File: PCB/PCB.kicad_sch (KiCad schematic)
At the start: 51 parts, among them J1 Conn_01x02_Socket, J2 Conn_01x02_Pin, J3 Conn_01x02_Pin, J4 Conn_01x02_Socket, J5 Programming Pin, J6 Programming Pin, J7 Programming Pin, J8 Programming Pin, U1 STM32L476RGTx, U2 FGPMMOPA6H, U4 TPS63001DRCR, U5 LM2735XMF/NOPB, U8 LM386, U9 MAX7375AXR805

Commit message: Add files via upload
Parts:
- removed FB1, FB4: FerriteBead, Ferrite_THT:LairdTech_28C0236-0JW-10, symbol Device:FerriteBead
- added R4, R5: 0 Ohms, symbol Device:R_US
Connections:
- net Earth: now also R4.1, R5.1
- net VDDA Connection: now also R4.2
- net VDDA GND Connection: now also R5.2
- net at U1.14 (PA0): no longer U2.P$10 (RX)
- net at U1.15 (PA1): no longer U2.P$9 (TX)
- net at U1.42 (PA9): now also U2.P$10 (RX)
- net at U1.43 (PA10): now also U2.P$9 (TX)
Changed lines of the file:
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@@
 	)
 	(no_connect
+		(at 186.69 80.01)
+	)
+	(no_connect
 		(at 186.69 153.67)
 	)
@@
 	)
 	(no_connect
-		(at 186.69 102.87)
-	)
-	(no_connect
 		(at 151.13 110.49)
 	)
@@
 	)
 	(no_connect
-		(at 186.69 105.41)
-	)
-	(no_connect
 		(at 151.13 138.43)
 	)
@@
 	)
 	(no_connect
+		(at 186.69 82.55)
+	)
+	(no_connect
 		(at 104.14 142.24)
 	)
@@
 	(wire
 		(pts
+			(xy 186.69 102.87) (xy 194.31 102.87)
+		)
+		(stroke
+			(width 0)
+			(type default)
+		)
+	)
+	(wire
+		(pts
 			(xy 194.31 179.07) (xy 67.31 179.07)
 		)
@@
 	(wire
 		(pts
+			(xy 190.5 105.41) (xy 190.5 177.8)
+		)
+		(stroke
+			(width 0)
+			(type default)
+		)
+	)
+	(wire
+		(pts
 			(xy 220.98 55.88) (xy 243.84 55.88)
 		)
@@
 	(wire
 		(pts
+			(xy 186.69 105.41) (xy 190.5 105.41)
+		)
+		(stroke
+			(width 0)
+			(type default)
+		)
+	)
+	(wire
+		(pts
 			(xy 181.61 24.13) (xy 223.52 24.13)
 		)
@@
 	(wire
 		(pts
-			(xy 190.5 82.55) (xy 190.5 177.8)
-		)
-		(stroke
-			(width 0)
-			(type default)
-		)
-	)
-	(wire
-		(pts
 			(xy 66.04 87.63) (xy 83.82 87.63)
 		)
@@
 	(wire
 		(pts
-			(xy 194.31 80.01) (xy 194.31 179.07)
-		)
-		(stroke
-			(width 0)
-			(type default)
-		)
-	)
-	(wire
-		(pts
 			(xy 43.18 46.99) (xy 48.26 46.99)
 		)
@@
 	(wire
 		(pts
+			(xy 194.31 102.87) (xy 194.31 179.07)
+		)
+		(stroke
+			(width 0)
+			(type default)
+		)
+	)
+	(wire
+		(pts
 			(xy 17.78 181.61) (xy 24.13 181.61)
 		)
@@
 	(wire
 		(pts
-			(xy 186.69 82.55) (xy 190.5 82.55)
-		)
-		(stroke
-			(width 0)
-			(type default)
-		)
-	)
-	(wire
-		(pts
 			(xy 171.45 72.39) (xy 176.53 72.39)
 		)
@@
 	(wire
 		(pts
-			(xy 186.69 80.01) (xy 194.31 80.01)
-		)
-		(stroke
-			(width 0)
-			(type default)
-		)
-	)
-	(wire
-		(pts
 			(xy 73.66 142.24) (xy 71.12 142.24)
 		)
@@
 	)
 	(symbol
-		(lib_id "Device:FerriteBead")
-		(at 245.11 153.67 90)
-		(unit 1)
-		(exclude_from_sim no)
-		(in_bom yes)
-		(on_board yes)
-		(dnp no)
-		(fields_autoplaced yes)
-		(property "Reference" "FB4"
-			(at 245.0592 146.05 90)
-			(effects
-				(font
-					(size 1.27 1.27)
-				)
-			)
-		)
-		(property "Value" "FerriteBead"
-			(at 245.0592 148.59 90)
-			(effects
-				(font
-					(size 1.27 1.27)
-				)
-			)
-		)
-		(property "Footprint" "Ferrite_THT:LairdTech_28C0236-0JW-10"
-			(at 245.11 155.448 90)
-			(effects
-				(font
-					(size 1.27 1.27)
-				)
-				(hide yes)
-			)
-		)
-		(property "Datasheet" "~"
-			(at 245.11 153.67 0)
-			(effects
-				(font
-					(size 1.27 1.27)
-				)
-				(hide yes)
-			)
-		)
-		(property "Description" ""
-			(at 245.11 153.67 0)
-			(effects
-				(font
-					(size 1.27 1.27)
-				)
-				(hide yes)
-			)
-		)
-		(pin "1"
-		)
-		(pin "2"
-		)
-		(instances
-			(project "PCB"
-				(path "/eb9a8801-b205-4599-90e8-b0089b4de1f9"
-					(reference "FB4")
-					(unit 1)
-				)
-			)
-		)
-	)
-	(symbol
 		(lib_id "Connector:Conn_01x02_Pin")
 		(at 21.59 10.16 270)
@@
 	)
 	(symbol
+		(lib_id "Device:R_US")
+		(at 245.11 153.67 90)
+		(unit 1)
+		(exclude_from_sim no)
+		(in_bom yes)
+		(on_board yes)
+		(dnp no)
+		(fields_autoplaced yes)
+		(property "Reference" "R5"
+			(at 245.11 147.32 90)
+			(effects
+				(font
+					(size 1.27 1.27)
+				)
+			)
+		)
+		(property "Value" "0 Ohms"
+			(at 245.11 149.86 90)
+			(effects
+				(font
+					(size 1.27 1.27)
+				)
+			)
+		)
+		(property "Footprint" ""
+			(at 245.364 152.654 90)
+			(effects
+				(font
+					(size 1.27 1.27)
+				)
+				(hide yes)
+			)
+		)
+		(property "Datasheet" "~"
+			(at 245.11 153.67 0)
+			(effects
+				(font
+					(size 1.27 1.27)
+				)
+				(hide yes)
+			)
+		)
+		(property "Description" "Resistor, US symbol"
+			(at 245.11 153.67 0)
+			(effects
+				(font
+					(size 1.27 1.27)
+				)
+				(hide yes)
+			)
+		)
+		(pin "2"
+		)
+		(pin "1"
+		)
+		(instances
+			(project "PCB"
+				(path "/eb9a8801-b205-4599-90e8-b0089b4de1f9"
+					(reference "R5")
+					(unit 1)
+				)
+			)
+		)
+	)
+	(symbol
 		(lib_id "Device:D_Schottky")
 		(at 252.73 17.78 180)
@@
 	)
 	(symbol
+		(lib_id "Device:R_US")
+		(at 243.84 143.51 90)
+		(unit 1)
+		(exclude_from_sim no)
+		(in_bom yes)
+		(on_board yes)
+		(dnp no)
+		(fields_autoplaced yes)
+		(property "Reference" "R4"
+			(at 243.84 137.16 90)
+			(effects
+				(font
+					(size 1.27 1.27)
+				)
+			)
+		)
+		(property "Value" "0 Ohms"
+			(at 243.84 139.7 90)
+			(effects
+				(font
+					(size 1.27 1.27)
+				)
+			)
+		)
+		(property "Footprint" ""
+			(at 244.094 142.494 90)
+			(effects
+				(font
+					(size 1.27 1.27)
+				)
+				(hide yes)
+			)
+		)
+		(property "Datasheet" "~"
+			(at 243.84 143.51 0)
+			(effects
+				(font
+					(size 1.27 1.27)
+				)
+				(hide yes)
+			)
+		)
+		(property "Description" "Resistor, US symbol"
+			(at 243.84 143.51 0)
+			(effects
+				(font
+					(size 1.27 1.27)
+				)
+				(hide yes)
+			)
+		)
+		(pin "2"
+		)
+		(pin "1"
+		)
+		(instances
+			(project ""
+				(path "/eb9a8801-b205-4599-90e8-b0089b4de1f9"
+					(reference "R4")
+					(unit 1)
+				)
+			)
+		)
+	)
+	(symbol
 		(lib_id "Buck-Boost Chip:TPS63001DRCR")
 		(at 66.04 62.23 0)
@@
 					(unit 1)
 				)
-			)
-		)
-	)
-	(symbol
-		(lib_id "Device:FerriteBead")
-		(at 243.84 143.51 90)
-		(unit 1)
-		(exclude_from_sim no)
-		(in_bom yes)
-		(on_board yes)
-		(dnp no)
-		(fields_autoplaced yes)
-		(property "Reference" "FB1"
-			(at 243.7892 135.89 90)
-			(effects
-				(font
-					(size 1.27 1.27)
-				)
-			)
-		)
-		(property "Value" "FerriteBead"
-			(at 243.7892 138.43 90)
-			(effects
-				(font
-					(size 1.27 1.27)
-				)
-			)
-		)
-		(property "Footprint" "Ferrite_THT:LairdTech_28C0236-0JW-10"
-			(at 243.84 145.288 90)
-			(effects
-				(font
-					(size 1.27 1.27)
-				)
-				(hide yes)
-			)
-		)
-		(property "Datasheet" "~"
-			(at 243.84 143.51 0)
-			(effects
-				(font
-					(size 1.27 1.27)
-				)
-				(hide yes)
-			)
-		)
-		(property "Description" ""
-			(at 243.84 143.51 0)
-			(effects
-				(font
-					(size 1.27 1.27)
-				)
-				(hide yes)
-			)
-		)
-		(pin "1"
-		)
-		(pin "2"
-		)
-		(instances
-			(project "PCB"
-				(path "/eb9a8801-b205-4599-90e8-b0089b4de1f9"
-					(reference "FB1")
-					(unit 1)
-				)

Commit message: changed pcb
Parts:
- added C20: .1 uF, Capacitor_SMD:C_0805_2012Metric_Pad1.18x1.45mm_HandSolder, symbol Device:C
- added D2, D4, D5, D6: LED, LED_SMD:LED_0805_2012Metric, symbol Device:LED
- added R6, R7, R8, R9: 1K Ohms, Resistor_SMD:R_0805_2012Metric, symbol Device:R_US
- added SW1: SW_Push, Button_Switch_THT:SW_PUSH_6mm_H5mm, symbol Switch:SW_Push
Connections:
- net Earth: now also C20.2, D2.1 (K), D4.1 (K), D5.1 (K), D6.1 (K), SW1.1
- net at U1.27 (PB1): now also R9.2
- net at U1.28 (PB2): now also R8.2
- net at U1.29 (PB10): now also R7.2
- net at U1.30 (PB11): now also R6.2
- net at J5.1 (Pin_1), U1.7 (NRST): now also C20.1, SW1.2
- new net: D6.2 (A), R9.1
- new net: D2.2 (A), R6.1
- new net: D5.2 (A), R8.1
- new net: D4.2 (A), R7.1
- no-connect marks 61 -> 57
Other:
- moved on the sheet: J5

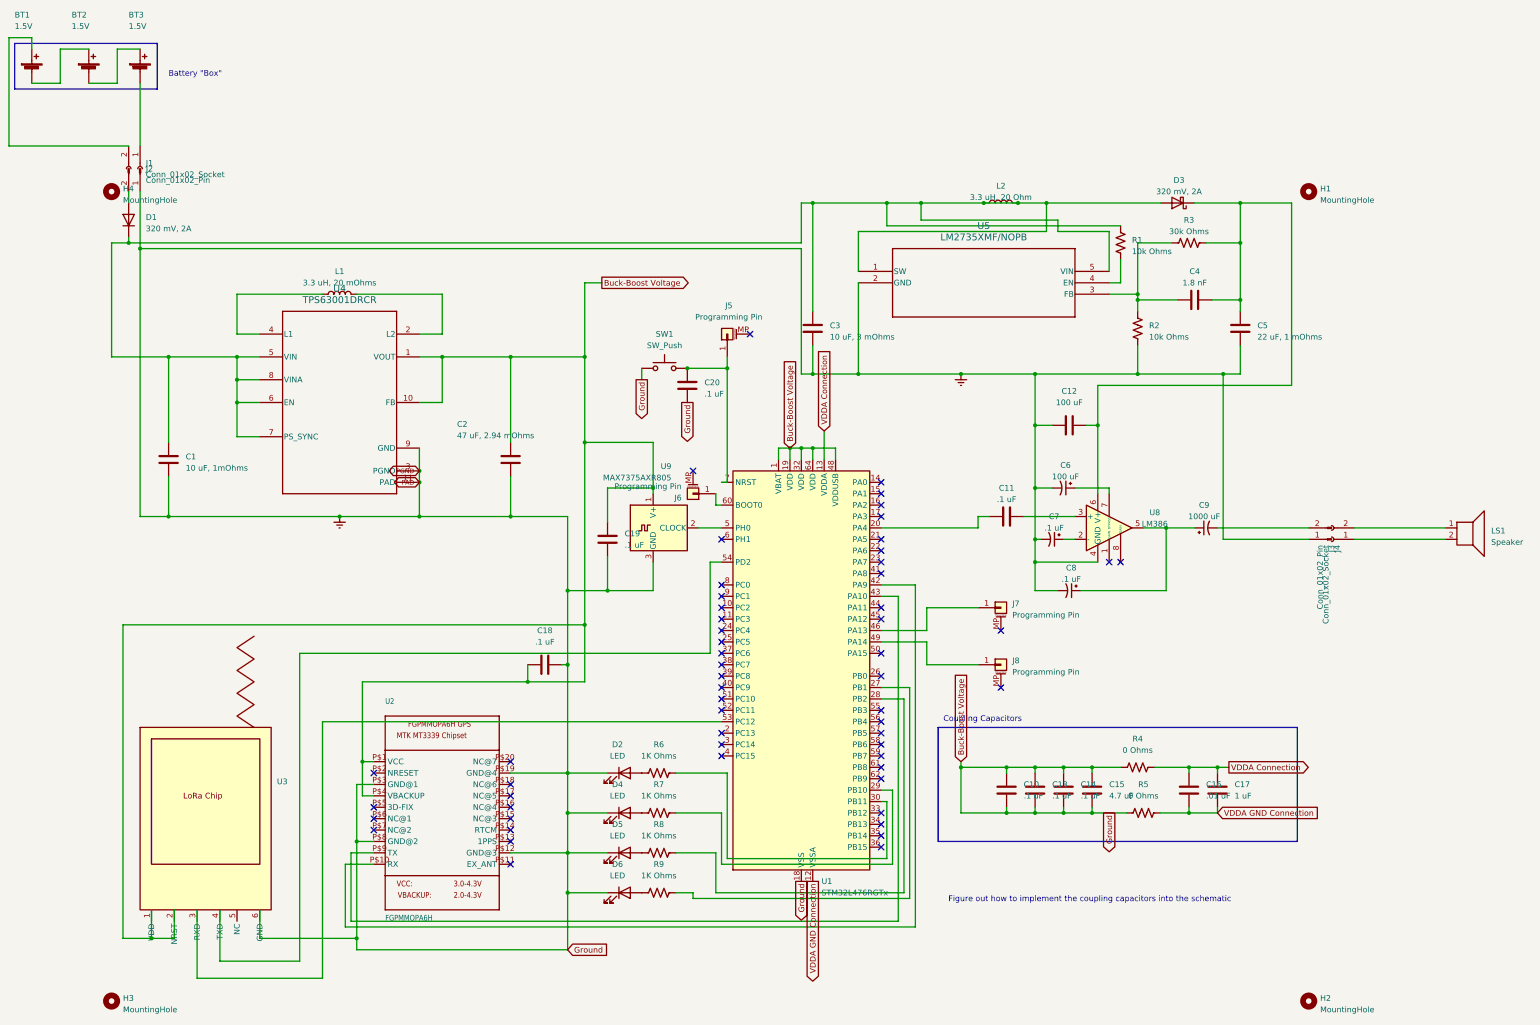
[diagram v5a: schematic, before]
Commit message: Added a few things for presentation purposes
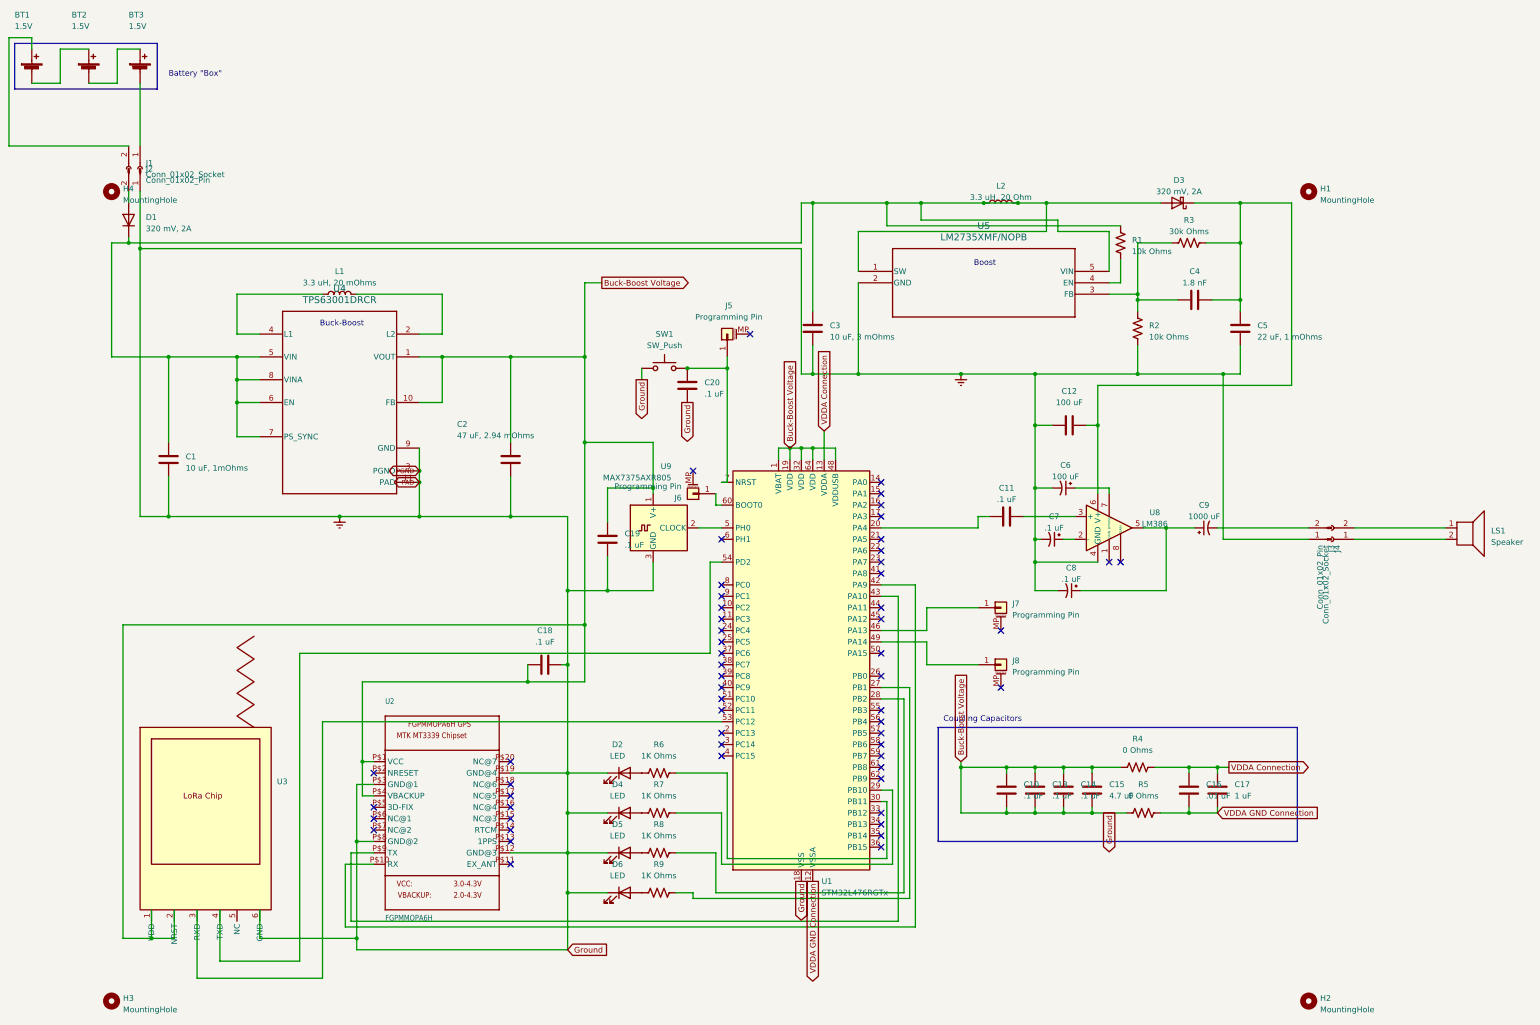
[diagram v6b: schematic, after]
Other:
- note added: "Boost"
- note added: "Buck-Boost"
- note removed: "Figure out how to implement the coupling capacitors into the schematic"
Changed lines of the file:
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@@
 		)
 	)
-	(text "Figure out how to implement the coupling capacitors into the schematic"
+	(text "Buck-Boost"
 		(exclude_from_sim no)
-		(at 233.172 172.974 0)
+		(at 66.548 44.704 0)
 		(effects
 			(font
+				(size 1.27 1.27)
+			)
+		)
+	)
+	(text "Boost\n"
+		(exclude_from_sim no)
+		(at 209.804 31.242 0)
+		(effects
+			(font
